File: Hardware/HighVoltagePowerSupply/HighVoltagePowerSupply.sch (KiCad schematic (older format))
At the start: 38 parts, among them Q3 Q_NMOS_GDS, Q8 Q_PMOS_GSD, Q9 Q_PMOS_GSD, U4 LM3488

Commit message: split (previousle one) pcb project to three separate pcbs
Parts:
- removed TR1: 750311771, GammaSpectrometer:750311771, symbol GammaSpectrometer:750311771
- removed U4: LM3488, Package_SO:VSSOP-8_2.4x2.1mm_P0.5mm, symbol GammaSpectrometer:LM3488
- added TR?: 750311771, HighVoltagePowerSupply:750311771, symbol HighVoltagePowerSupply:750311771
- added U?: LM3488, Package_SO:VSSOP-8_2.4x2.1mm_P0.5mm, symbol HighVoltagePowerSupply:LM3488
- L5: footprint GammaSpectrometer:L_7.3x7.3_H3.5 -> DataAcquisition:L_7.3x7.3_H3.5
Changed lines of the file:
@@
 $Descr A4 11693 8268
 encoding utf-8
-Sheet 3 7
+Sheet 1 1
 Title ""
 Date ""
@@
 Comment4 ""
 $EndDescr
-$Comp
-L GammaSpectrometer:LM3488 U4
-U 1 1 5EDBA656
-P 3950 3100
-F 0 "U4" H 3950 2600 50  0000 C CNN
-F 1 "LM3488" H 3950 2500 50  0000 C CNN
-F 2 "Package_SO:VSSOP-8_2.4x2.1mm_P0.5mm" H 3950 3100 50  0001 C CNN
-F 3 "https://www.ti.com/lit/ds/symlink/lm3488.pdf?ts=1591443135460&ref_url=https://www.ti.com/store/ti/en/p/product/?p%3DLM3488MM" H 3950 3100 50  0001 C CNN
-	1    3950 3100
-	1    0    0    -1
-$EndComp
 $Comp
 L Device:Q_NMOS_GDS Q3
@@
 	8900 1950 9000 1950
 Connection ~ 9000 1950
-$Comp
-L GammaSpectrometer:750311771 TR1
-U 1 1 5EF92A84
-P 6150 1900
-F 0 "TR1" H 6250 2075 50  0000 C CNN
-F 1 "750311771" H 6250 1984 50  0000 C CNN
-F 2 "GammaSpectrometer:750311771" H 6150 2050 50  0001 C CNN
-F 3 "http://www.farnell.com/datasheets/1337718.pdf?_ga=2.65563566.1225228608.1593261089-1855792729.1592068583" H 6150 2050 50  0001 C CNN
-	1    6150 1900
-	-1   0    0    -1
-$EndComp
 Connection ~ 7350 2600
 Connection ~ 7900 2600
@@
 F 0 "L5" V 1825 1850 50  0000 C CNN
 F 1 "L_Core_Ferrite" V 1734 1850 50  0000 C CNN
-F 2 "GammaSpectrometer:L_7.3x7.3_H3.5" H 1600 1850 50  0001 C CNN
+F 2 "DataAcquisition:L_7.3x7.3_H3.5" H 1600 1850 50  0001 C CNN
 F 3 "~" H 1600 1850 50  0001 C CNN
 	1    1600 1850
@@
 Text Label 1300 5950 1    50   ~ 0
 12V_HV_PowerSupply
+$Comp
+L HighVoltagePowerSupply:750311771 TR?
+U 1 1 5FA1AC0B
+P 6150 1900
+F 0 "TR?" H 6250 2075 50  0000 C CNN
+F 1 "750311771" H 6250 1984 50  0000 C CNN
+F 2 "HighVoltagePowerSupply:750311771" H 6150 2050 50  0001 C CNN
+F 3 "" H 6150 2050 50  0001 C CNN
+	1    6150 1900
+	-1   0    0    -1
+$EndComp
+$Comp
+L HighVoltagePowerSupply:LM3488 U?
+U 1 1 5FA1EE2B
+P 3950 3100
+F 0 "U?" H 3950 3225 50  0000 C CNN
+F 1 "LM3488" H 3950 3134 50  0000 C CNN
+F 2 "Package_SO:VSSOP-8_2.4x2.1mm_P0.5mm" H 3950 3100 50  0001 C CNN
+F 3 "" H 3950 3100 50  0001 C CNN
+	1    3950 3100
+	1    0    0    -1
+$EndComp
 $EndSCHEMATC

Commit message: add calculation of (some) components of LT3580 (chip used to generate high voltage for photomultiplier). Update README.md about used microcontroler and user interface, paritialy create circuit for high voltage generator.
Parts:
- removed C12, C52: 100n, Capacitor_SMD:C_0805_2012Metric_Pad1.15x1.40mm_HandSolder, symbol Device:C
- removed C50, C51: 220u, Capacitor_SMD:CP_Elec_6.3x5.8, symbol Device:CP
- removed C8: 10n, Capacitor_SMD:C_0805_2012Metric_Pad1.15x1.40mm_HandSolder, symbol Device:C
- removed D4: red, LED_SMD:LED_0805_2012Metric, symbol Device:LED
- removed L5: L_Core_Ferrite, DataAcquisition:L_7.3x7.3_H3.5, symbol Device:L_Core_Ferrite
- removed Q3: Q_NMOS_GDS, Package_TO_SOT_THT:TO-220-3_Horizontal_TabDown, symbol Device:Q_NMOS_GDS
- removed Q8, Q9: Q_PMOS_GSD, Package_TO_SOT_SMD:SOT-23, symbol Device:Q_PMOS_GSD
- removed R67, R68: 10k, Resistor_SMD:R_0805_2012Metric_Pad1.15x1.40mm_HandSolder, symbol Device:R
- removed TR?: 750311771, HighVoltagePowerSupply:750311771, symbol HighVoltagePowerSupply:750311771
- removed U?: LM3488, Package_SO:VSSOP-8_2.4x2.1mm_P0.5mm, symbol HighVoltagePowerSupply:LM3488
- added C1, C18, C19, C2, C20, C21, C22, C23, C24, C25, C26, C27, C28, C29, C30, C31, C32, C33, C34, C35, C36, C37, C38, C39, C4, C40, C41, C5, C6: 100p, Capacitor_SMD:C_0805_2012Metric_Pad1.15x1.40mm_HandSolder, symbol Device:C
- added C12, C42, C8: 220u, Capacitor_SMD:CP_Elec_6.3x5.8, symbol Device:CP
- added C43, C44, C45, C46, C47, C48: 100n, Capacitor_SMD:C_0805_2012Metric_Pad1.15x1.40mm_HandSolder, symbol Device:C
- added D1, D10, D11, D12, D13, D14, D15, D16, D17, D18, D19, D2, D20, D21, D22, D23, D24, D25, D6, D7, D8, D9: D, Diode_SMD:D_MELF, symbol Device:D
- added J1: Conn_01x02_Female, symbol Connector:Conn_01x02_Female
- added J10, J11, J12, J13, J14, J2, J3, J4, J5, J6, J7, J8, J9: Conn_01x01_Male, symbol Connector:Conn_01x01_Male
- added J15: Conn_01x03_Female, symbol Connector:Conn_01x03_Female
- added JP1: Jumper_NC_Small, symbol Device:Jumper_NC_Small
- added L1, L2, L3: L_Core_Ferrite, DataAcquisition:L_7.3x7.3_H3.5, symbol Device:L_Core_Ferrite
- added Q1: BC848, Package_TO_SOT_SMD:SOT-23, symbol Transistor_BJT:BC848
- added R1, R11, R2, R4, R5, R7, R8, R9: 150k, Resistor_THT:R_Axial_DIN0207_L6.3mm_D2.5mm_P10.16mm_Horizontal, symbol Device:R
- added R15, R31: 10k, Resistor_SMD:R_0805_2012Metric_Pad1.15x1.40mm_HandSolder, symbol Device:R
- added R22, R23, R24, R25, R26, R27, R28, R29, R30: 10M, Resistor_SMD:R_0805_2012Metric_Pad1.15x1.40mm_HandSolder, symbol Device:R
- added TP1, TP2, TP3, TP4: TestPoint, symbol Connector:TestPoint
- added TR1: TRANSF2, symbol Transformer:TRANSF2
- added U1: LT3580xMS8E, Package_SO:MSOP-8-1EP_3x3mm_P0.65mm_EP1.68x1.88mm, symbol Regulator_Switching:LT3580xMS8E
- added U2: LM358, symbol Amplifier_Operational:LM358
- C14, C15, C16, C17: value 10n/2kV -> 100p; footprint Capacitor_THT:C_Disc_D11.0mm_W5.0mm_P10.00mm -> Capacitor_SMD:C_0805_2012Metric_Pad1.15x1.40mm_HandSolder
- C3: value 10n/3kV -> 100p; footprint Capacitor_THT:C_Disc_D11.0mm_W5.0mm_P10.00mm -> Capacitor_SMD:C_0805_2012Metric_Pad1.15x1.40mm_HandSolder
- C9: value 10n -> 100p
- D5: footprint Diode_THT:D_DO-27_P15.24mm_Horizontal -> Diode_SMD:D_MELF
- R10, R3, R6: value 510R -> 150k; footprint Resistor_SMD:R_MELF_MMB-0207 -> Resistor_THT:R_Axial_DIN0207_L6.3mm_D2.5mm_P10.16mm_Horizontal
- R12: value 0R -> 150k; footprint Resistor_SMD:R_0805_2012Metric_Pad1.15x1.40mm_HandSolder -> Resistor_THT:R_Axial_DIN0207_L6.3mm_D2.5mm_P10.16mm_Horizontal
- R14: value 150k -> 10k; footprint Resistor_THT:R_Axial_DIN0207_L6.3mm_D2.5mm_P10.16mm_Horizontal -> Resistor_SMD:R_0805_2012Metric_Pad1.15x1.40mm_HandSolder
- R16: value 1k -> 10k
- R20: footprint Resistor_SMD:R_MELF_MMB-0207 -> Resistor_SMD:R_0805_2012Metric_Pad1.15x1.40mm_HandSolder
- R21: value 10k -> 10M; footprint Resistor_SMD:R_MELF_MMB-0207 -> Resistor_SMD:R_0805_2012Metric_Pad1.15x1.40mm_HandSolder
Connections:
- net labels added: ENABLE, HV_MONITOR, V_DIVIDER
- net labels removed: 12V_HV_PowerSupply, HV_EN, TUBE_POWER_SUPPLY_NEGATIVE, TUBE_POWER_SUPPLY_POSITIVE, VCC
- wire segments 127 -> 347
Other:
- note added: "Place C8, C11, C45, C46, C47, L1 close to TR1.\nPlace C12, C43, L2 close to pin #3 of U1.\nPlace C42, C44, L3 close U2C.\n"
- note removed: "Place C10-C12 close to TR1."

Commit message: finish model to calculate dc/dc converter element values, fix way how dc/dc chip is turned on/off, add current monitoring to dc/dc converter pcb, so that it will be possible to turn it off if the output voltage/input current is too high (fix: #60)
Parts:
- removed Q1: BC848, Package_TO_SOT_SMD:SOT-23, symbol Transistor_BJT:BC848
- added J?: Conn_01x02_Female, symbol Connector:Conn_01x02_Female
- added Q1: BC859, Package_TO_SOT_SMD:SOT-23, symbol Transistor_BJT:BC859
- added R32, R?: 10k, Resistor_SMD:R_0805_2012Metric_Pad1.15x1.40mm_HandSolder, symbol Device:R
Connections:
- wire segments 347 -> 364
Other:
- moved on the sheet: C10, C11, C12, C42, C43, C44, C45, C46, C47, C48, C7, C8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

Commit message: add correct footprints to some of components, add basic placement of components on pcb
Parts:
- removed D1, D10, D11, D12, D13, D14, D15, D16, D17, D18, D19, D2, D20, D21, D22, D23, D24, D25, D3, D5, D6, D7, D8, D9: D, Diode_SMD:D_MELF, symbol Device:D
- added C49: 100n, Capacitor_SMD:C_0805_2012Metric_Pad1.15x1.40mm_HandSolder, symbol Device:C
- added D1, D10, D11, D12, D13, D14, D15, D16, D17, D18, D19, D2, D20, D21, D22, D23, D24, D3, D4, D5, D6, D7, D8, D9: SS220, Diode_SMD:D_SMB, symbol Device:D_Schottky
- C1, C13, C14, C15, C16, C17, C18, C19, C2, C20, C21, C22, C23, C24, C25, C26, C27, C28, C29, C3, C30, C31, C32, C33, C34, C35, C36, C37, C38, C39, C4, C40, C41, C5, C6, C9: footprint Capacitor_SMD:C_0805_2012Metric_Pad1.15x1.40mm_HandSolder -> Capacitor_SMD:C_1206_3216Metric
- J10, J11, J12, J13, J14, J2, J3, J4, J5, J6, J7, J8, J9: footprint (none) -> TestPoint:TestPoint_Loop_D2.54mm_Drill1.5mm_Beaded
- JP1: footprint (none) -> Jumper:SolderJumper-2_P1.3mm_Bridged2Bar_Pad1.0x1.5mm
- L2, L3: value L_Core_Ferrite -> 12u
- R1, R10, R11, R12, R13, R2, R3, R4, R5, R6, R7, R8, R9: footprint Resistor_THT:R_Axial_DIN0207_L6.3mm_D2.5mm_P10.16mm_Horizontal -> Resistor_SMD:R_0805_2012Metric
- R14, R15, R16, R19, R20, R31, R32: footprint Resistor_SMD:R_0805_2012Metric_Pad1.15x1.40mm_HandSolder -> Resistor_SMD:R_0805_2012Metric
- R17, R18, R21, R22, R23, R24, R25, R26, R27, R28, R29, R30: footprint Resistor_SMD:R_0805_2012Metric_Pad1.15x1.40mm_HandSolder -> Resistor_THT:R_Axial_DIN0207_L6.3mm_D2.5mm_P10.16mm_Horizontal
- R33: renamed from R?; footprint Resistor_SMD:R_0805_2012Metric_Pad1.15x1.40mm_HandSolder -> Resistor_SMD:R_0805_2012Metric
- TP1, TP2, TP3, TP4: footprint (none) -> TestPoint:TestPoint_Pad_D2.5mm
- gave numbers to parts that had none: 1
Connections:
- wire segments 364 -> 370

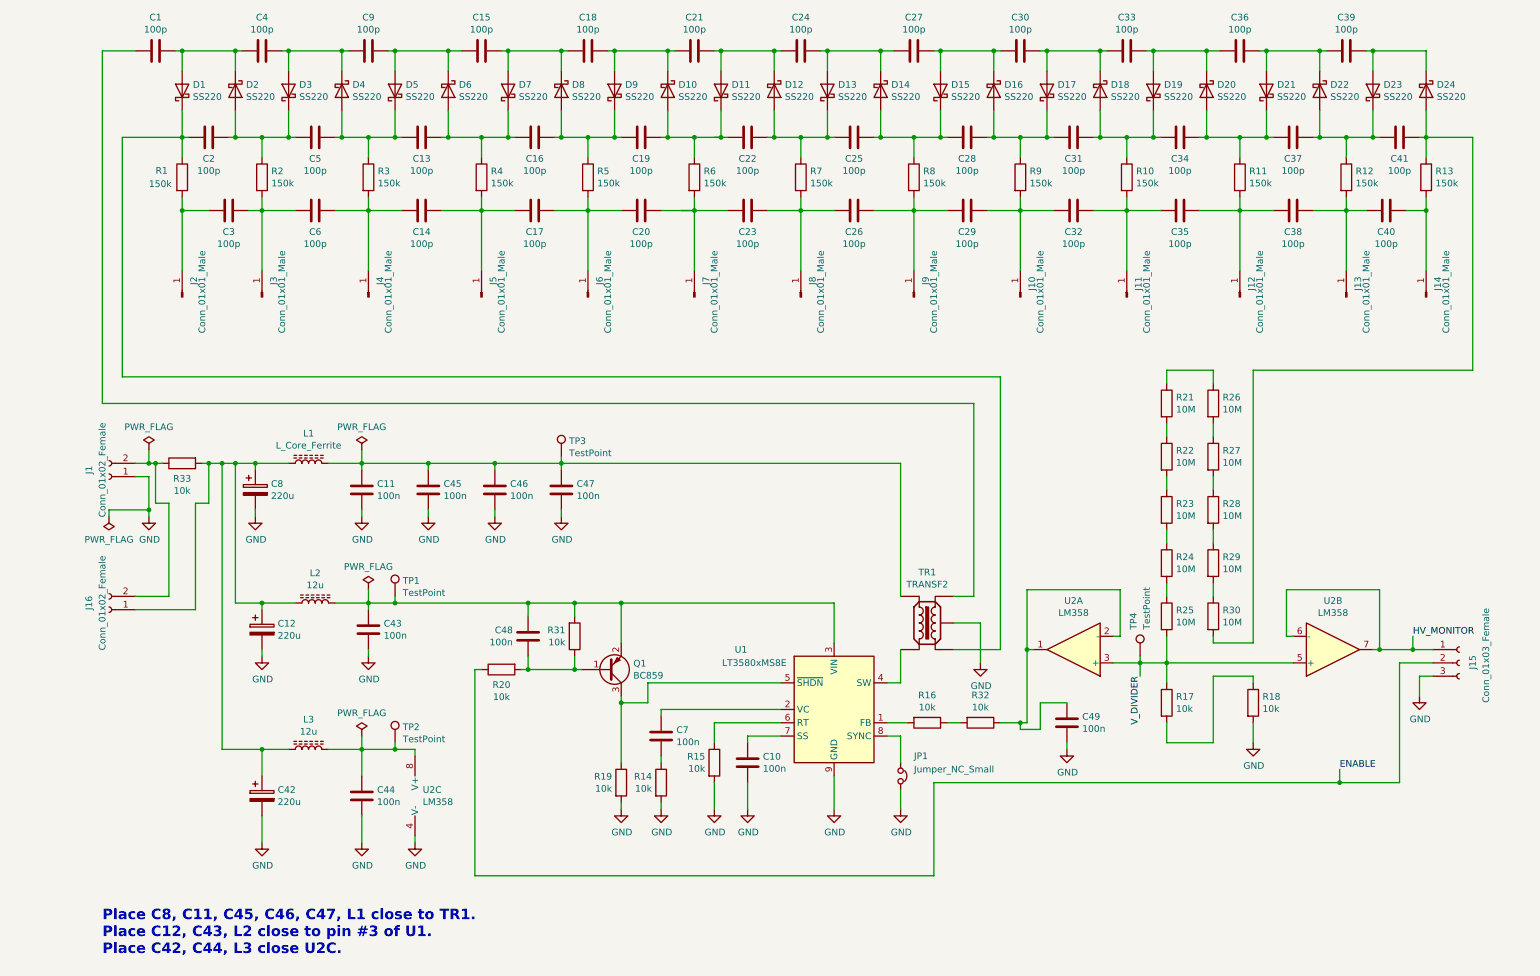
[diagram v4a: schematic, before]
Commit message: Choose op-amp for hv power supply board (fix: #67)
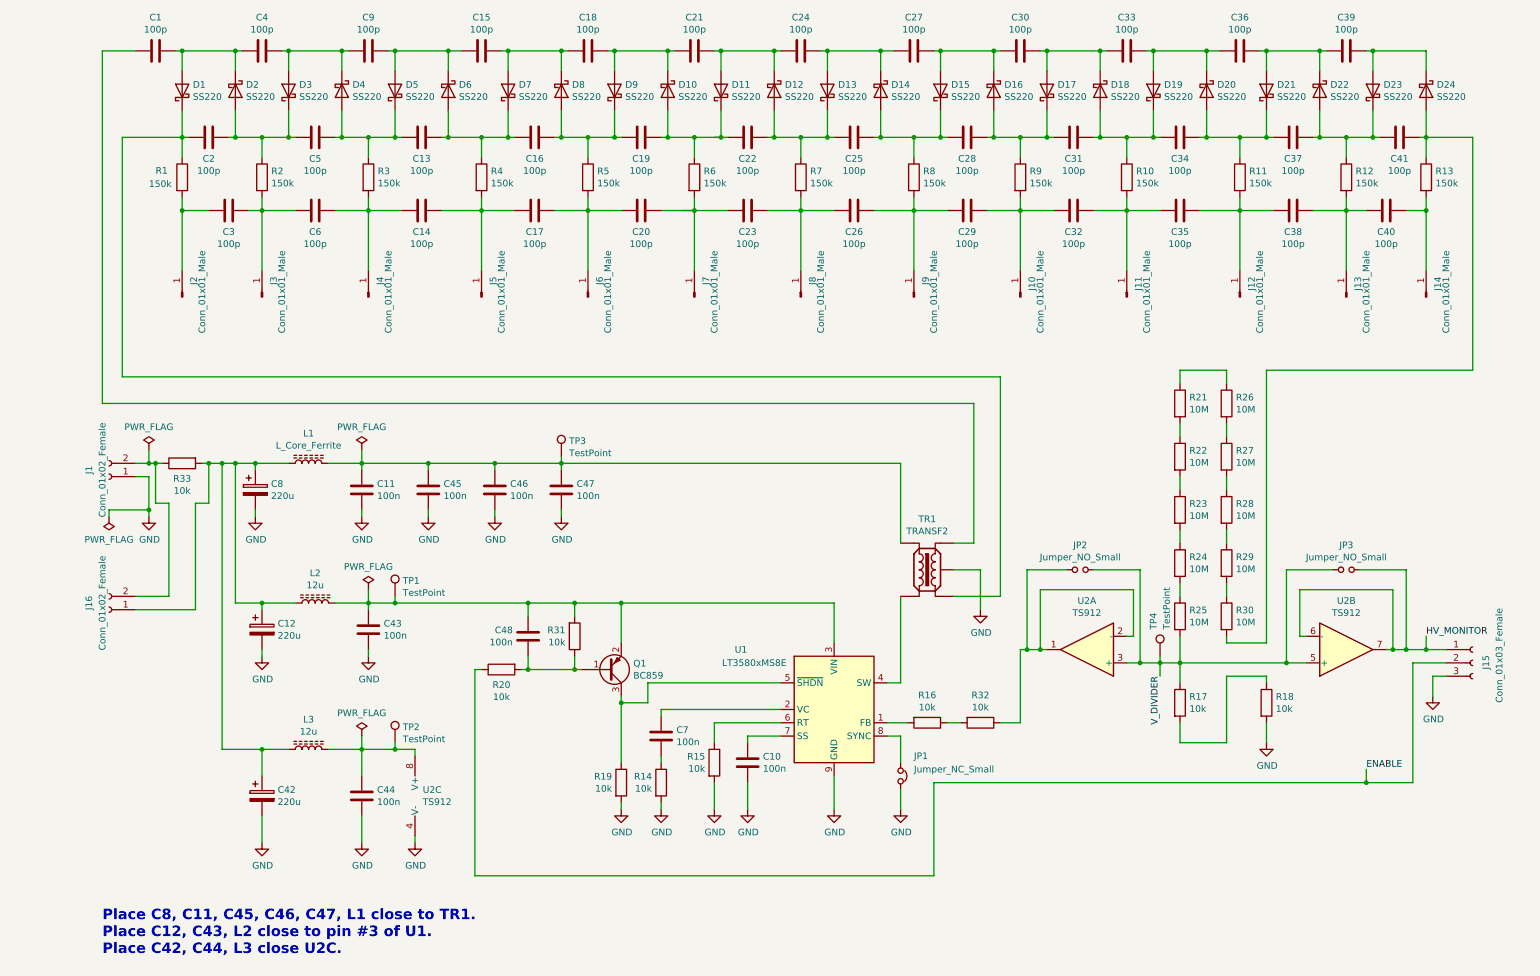
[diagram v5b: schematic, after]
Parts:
- removed C49: 100n, Capacitor_SMD:C_0805_2012Metric_Pad1.15x1.40mm_HandSolder, symbol Device:C
- removed U2: LM358, symbol Amplifier_Operational:LM358
- added JP2, JP3: Jumper_NO_Small, Jumper:SolderJumper-2_P1.3mm_Open_Pad1.0x1.5mm, symbol Device:Jumper_NO_Small
- added U2: TS912, Package_SO:SO-8_3.9x4.9mm_P1.27mm, symbol Amplifier_Operational:TS912
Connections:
- net GND: now also U2.4 (V-)
- net HV_MONITOR: now also JP3.2, U2.6 (-), U2.7
- net V_DIVIDER: now also JP2.2, JP3.1, U2.3 (+), U2.5 (+)
- net at R32.1: now also JP2.1, U2.1, U2.2 (-)
- net at C44.2, L3.2, TP2.1: now also U2.8 (V+)
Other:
- moved on the sheet: J15, R17, R18, R21, R22, R23, R24, R25, R26, R27, R28, R29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

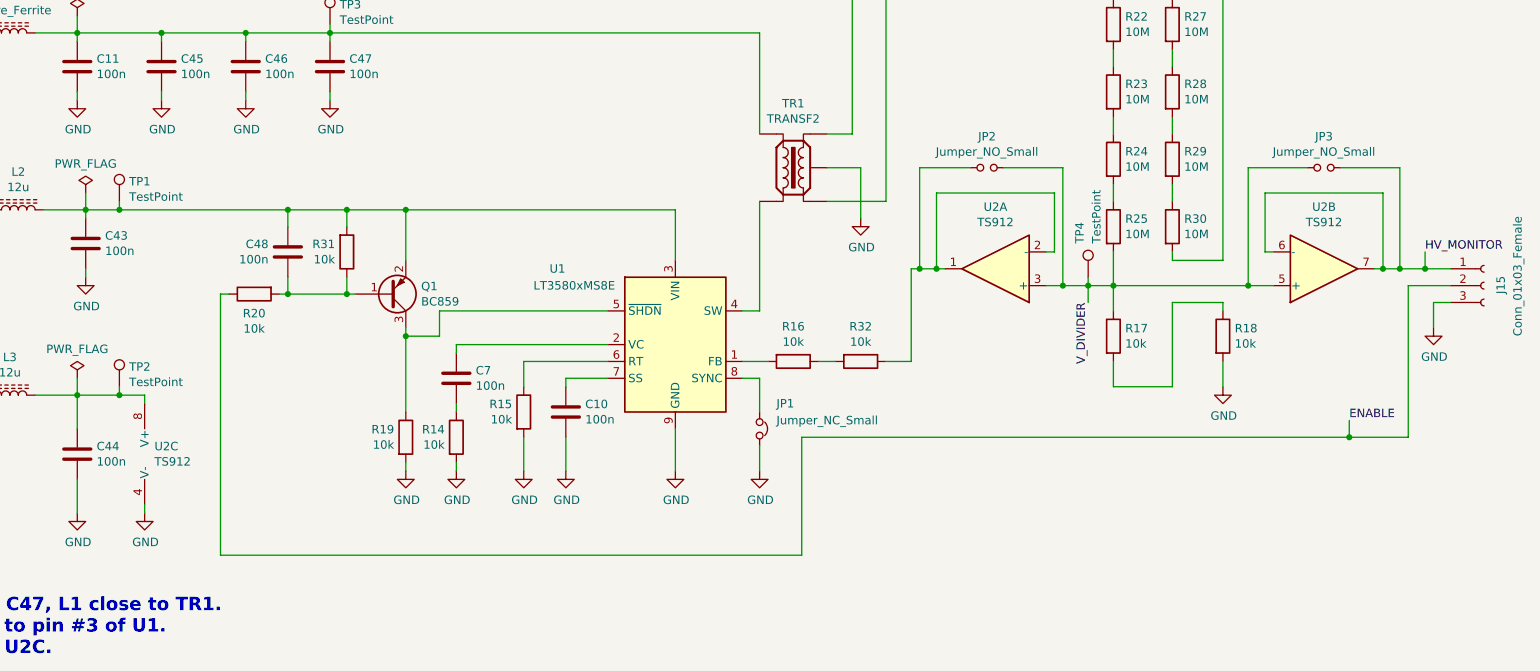
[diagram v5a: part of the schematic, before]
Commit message: Need unity gain opampfor opamp buffer, MCP6V51 choosed
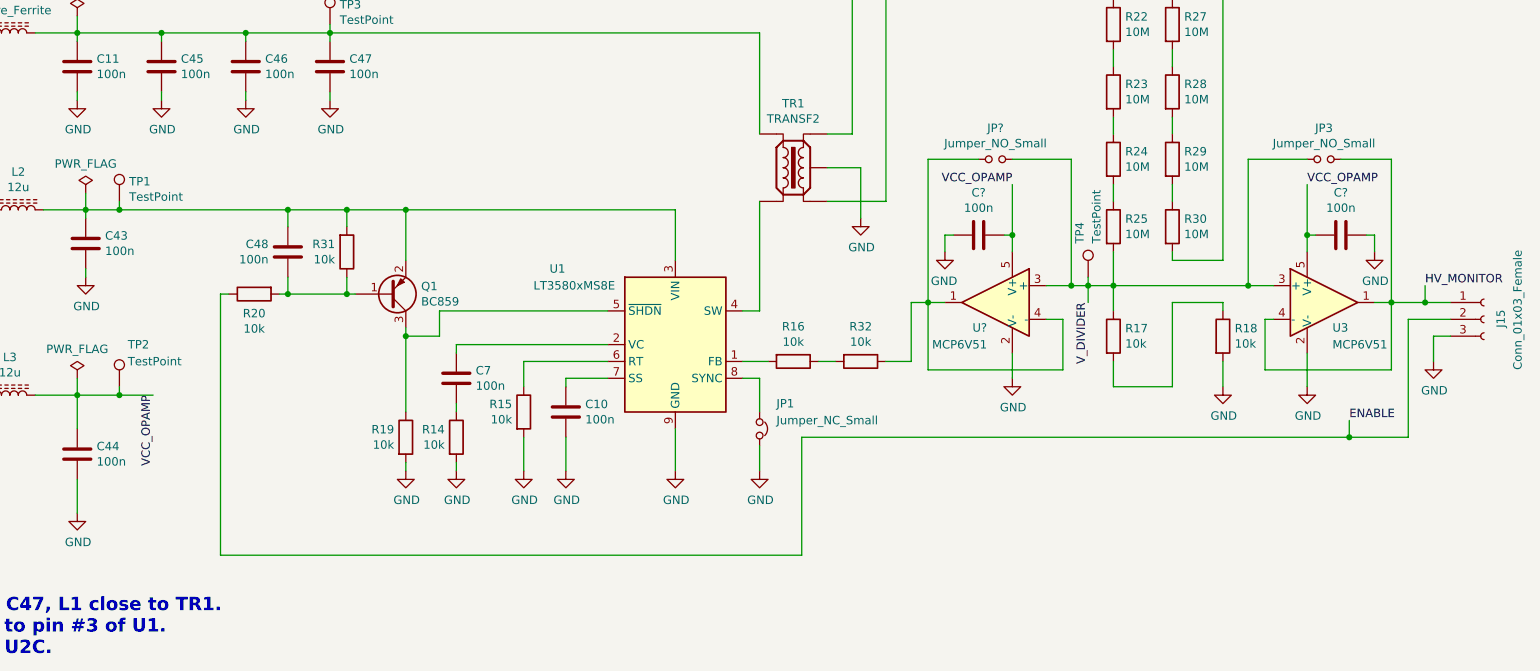
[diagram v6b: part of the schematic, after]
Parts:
- removed JP2: Jumper_NO_Small, Jumper:SolderJumper-2_P1.3mm_Open_Pad1.0x1.5mm, symbol Device:Jumper_NO_Small
- removed U2: TS912, Package_SO:SO-8_3.9x4.9mm_P1.27mm, symbol Amplifier_Operational:TS912
- added C? (x2): 100n, Capacitor_SMD:C_0805_2012Metric_Pad1.15x1.40mm_HandSolder, symbol Device:C
- added JP?: Jumper_NO_Small, Jumper:SolderJumper-2_P1.3mm_Open_Pad1.0x1.5mm, symbol Device:Jumper_NO_Small
- added U3, U?: MCP6V51, Package_TO_SOT_SMD:SOT-23-5, symbol HighVoltagePowerSupply:MCP6V51
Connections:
- net GND: now also C?.2, C?.2, U3.2 (V-), U?.2 (V-)
- net HV_MONITOR: now also U3.1, U3.4 (-)
- net V_DIVIDER: now also JP?.1, U3.3 (+), U?.3 (+)
- net at R32.1: now also JP?.2, U?.1, U?.4 (-)
- net VCC_OPAMP: now reaches C44.2, L3.2, TP2.1
- net VCC_OPAMP: now also C?.1, C?.1, U3.5 (V+), U?.5 (V+)
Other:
- moved on the sheet: J15, JP3
